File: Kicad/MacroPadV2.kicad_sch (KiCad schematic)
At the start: 31 parts, among them K1 KSW, K10 KSW, K11 KSW, K12 KSW, K2 KSW, K3 KSW, K4 KSW, K5 KSW, K6 KSW, K7 KSW, K8 KSW, K9 KSW, SW1 RotaryEncoder_Switch, U1 SparkFunProMicro

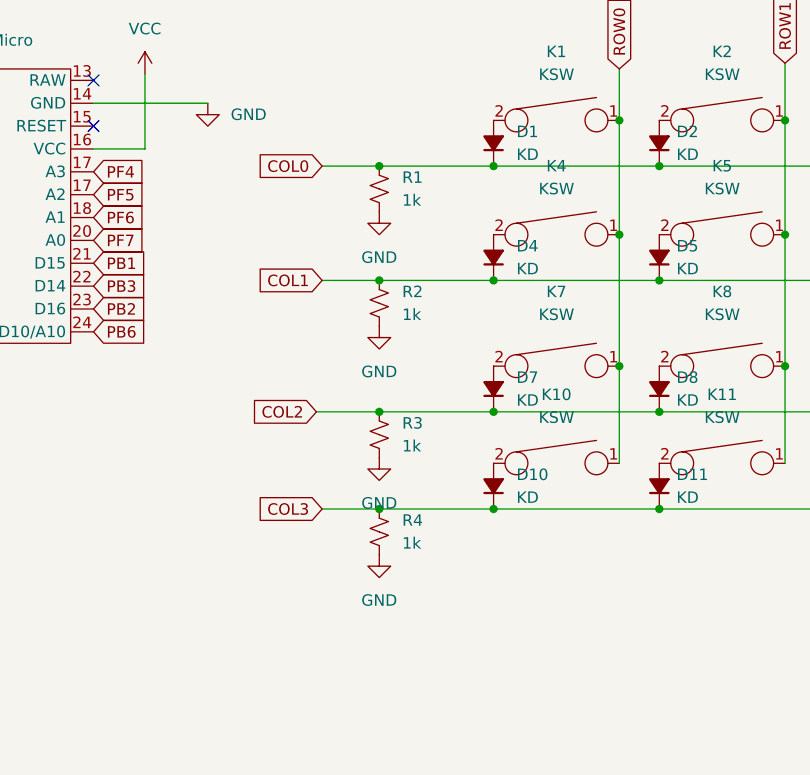
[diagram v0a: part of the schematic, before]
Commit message: Edit: IM AN IDIOT 	-ROWS ARE THE INPUTS, COLS ARE THE OUTPUTS 	-Set Cols Low to read a set, then all high after 	-Removed Pull down resistors on cols
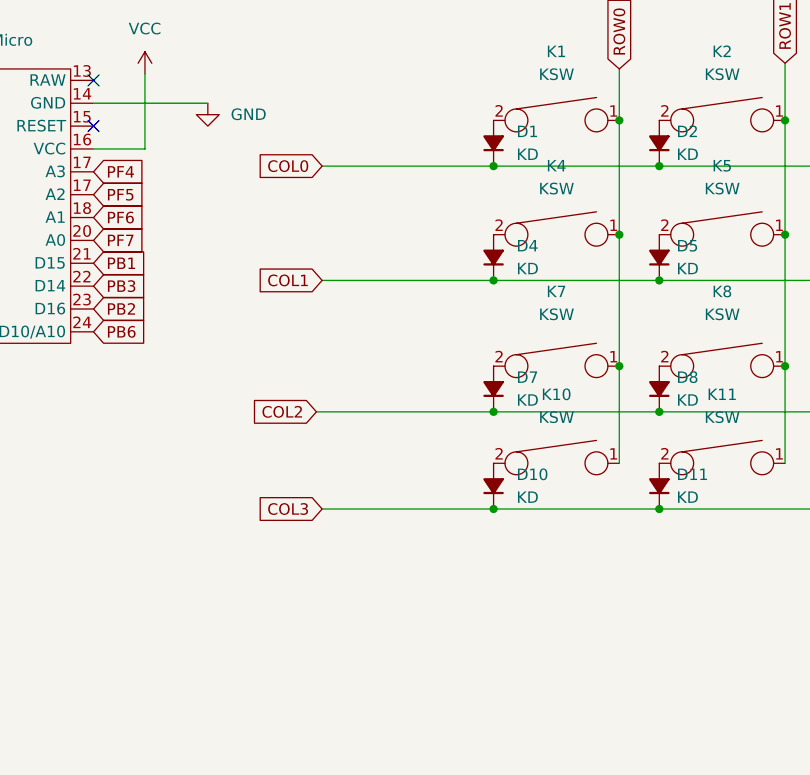
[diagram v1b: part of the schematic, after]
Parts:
- removed R1, R2, R3, R4: 1k, Resistor_SMD:R_0805_2012Metric_Pad1.20x1.40mm_HandSolder, symbol Device:R_Small_US
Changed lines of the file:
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@@
   (junction (at 120.65 29.21) (diameter 0) (color 0 0 0 0)
   )
-  (junction (at 93.98 72.39) (diameter 0) (color 0 0 0 0)
-  )
-  (junction (at 93.98 34.29) (diameter 0) (color 0 0 0 0)
-  )
   (junction (at 125.095 72.39) (diameter 0) (color 0 0 0 0)
   )
@@
   (junction (at 106.68 72.39) (diameter 0) (color 0 0 0 0)
   )
-  (junction (at 93.98 46.99) (diameter 0) (color 0 0 0 0)
-  )
   (junction (at 157.48 56.515) (diameter 0) (color 0 0 0 0)
-  )
-  (junction (at 93.98 61.595) (diameter 0) (color 0 0 0 0)
   )
   (junction (at 157.48 29.21) (diameter 0) (color 0 0 0 0)
@@
     (stroke (width 0) (type default) (color 0 0 0 0))
   )
-  (wire (pts (xy 93.98 72.39) (xy 106.68 72.39))
-    (stroke (width 0) (type default) (color 0 0 0 0))
-  )
   (wire (pts (xy 106.68 72.39) (xy 125.095 72.39))
     (stroke (width 0) (type default) (color 0 0 0 0))
@@
     (stroke (width 0) (type default) (color 0 0 0 0))
   )
-  (wire (pts (xy 93.98 46.99) (xy 106.68 46.99))
-    (stroke (width 0) (type default) (color 0 0 0 0))
-  )
   (wire (pts (xy 199.39 33.02) (xy 199.39 31.75))
     (stroke (width 0) (type default) (color 0 0 0 0))
   )
-  (wire (pts (xy 93.98 34.29) (xy 106.68 34.29))
-    (stroke (width 0) (type default) (color 0 0 0 0))
-  )
   (wire (pts (xy 157.48 41.91) (xy 157.48 56.515))
     (stroke (width 0) (type default) (color 0 0 0 0))
@@
     (stroke (width 0) (type default) (color 0 0 0 0))
   )
-  (wire (pts (xy 87.63 34.29) (xy 93.98 34.29))
+  (wire (pts (xy 87.63 34.29) (xy 106.68 34.29))
     (stroke (width 0) (type default) (color 0 0 0 0))
   )
@@
     (stroke (width 0) (type default) (color 0 0 0 0))
   )
-  (wire (pts (xy 87.63 46.99) (xy 93.98 46.99))
+  (wire (pts (xy 87.63 46.99) (xy 106.68 46.99))
     (stroke (width 0) (type default) (color 0 0 0 0))
   )
@@
     (stroke (width 0) (type default) (color 0 0 0 0))
   )
-  (wire (pts (xy 87.63 72.39) (xy 93.98 72.39))
+  (wire (pts (xy 87.63 72.39) (xy 106.68 72.39))
     (stroke (width 0) (type default) (color 0 0 0 0))
   )
@@
     (stroke (width 0) (type default) (color 0 0 0 0))
   )
-  (wire (pts (xy 86.995 61.595) (xy 93.98 61.595))
-    (stroke (width 0) (type default) (color 0 0 0 0))
-  )
-  (wire (pts (xy 93.98 61.595) (xy 106.68 61.595))
+  (wire (pts (xy 86.995 61.595) (xy 106.68 61.595))
     (stroke (width 0) (type default) (color 0 0 0 0))
   )
@@
     (pin "2")
   )
-  (symbol (lib_id "power:GND") (at 93.98 52.07 0) (unit 1)
-    (in_bom yes) (on_board yes) (fields_autoplaced)
-    (property "Reference" "#PWR0106" (id 0) (at 93.98 58.42 0)
-      (effects (font (size 1.27 1.27)) hide)
-    )
-    (property "Value" "GND" (id 1) (at 93.98 57.15 0))
-    (property "Footprint" "" (id 2) (at 93.98 52.07 0)
-      (effects (font (size 1.27 1.27)) hide)
-    )
-    (property "Datasheet" "" (id 3) (at 93.98 52.07 0)
-      (effects (font (size 1.27 1.27)) hide)
-    )
-    (pin "1")
-  )
   (symbol (lib_id "Device:D_Small_Filled") (at 125.095 31.75 90) (unit 1)
     (in_bom yes) (on_board yes) (fields_autoplaced)
@@
     (pin "1")
     (pin "2")
-  )
-  (symbol (lib_id "power:GND") (at 93.98 77.47 0) (unit 1)
-    (in_bom yes) (on_board yes) (fields_autoplaced)
-    (property "Reference" "#PWR0108" (id 0) (at 93.98 83.82 0)
-      (effects (font (size 1.27 1.27)) hide)
-    )
-    (property "Value" "GND" (id 1) (at 93.98 82.55 0))
-    (property "Footprint" "" (id 2) (at 93.98 77.47 0)
-      (effects (font (size 1.27 1.27)) hide)
-    )
-    (property "Datasheet" "" (id 3) (at 93.98 77.47 0)
-      (effects (font (size 1.27 1.27)) hide)
-    )
-    (pin "1")
   )
   (symbol (lib_id "macropad_parts:KSW") (at 119.38 36.83 0) (unit 1)
@@
     (pin "1")
   )
-  (symbol (lib_id "Device:R_Small_US") (at 93.98 36.83 0) (unit 1)
-    (in_bom yes) (on_board yes) (fields_autoplaced)
-    (property "Reference" "R1" (id 0) (at 96.52 35.5599 0)
-      (effects (font (size 1.27 1.27)) (justify left))
-    )
-    (property "Value" "1k" (id 1) (at 96.52 38.0999 0)
-      (effects (font (size 1.27 1.27)) (justify left))
-    )
-    (property "Footprint" "Resistor_SMD:R_0805_2012Metric_Pad1.20x1.40mm_HandSolder" (id 2) (at 93.98 36.83 0)
-      (effects (font (size 1.27 1.27)) hide)
-    )
-    (property "Datasheet" "~" (id 3) (at 93.98 36.83 0)
-      (effects (font (size 1.27 1.27)) hide)
-    )
-    (pin "1")
-    (pin "2")
-  )
   (symbol (lib_id "macropad_parts:KSW") (at 156.21 62.23 0) (unit 1)
     (in_bom yes) (on_board yes) (fields_autoplaced)
@@
     (pin "2")
   )
-  (symbol (lib_id "power:GND") (at 93.98 39.37 0) (unit 1)
-    (in_bom yes) (on_board yes) (fields_autoplaced)
-    (property "Reference" "#PWR0109" (id 0) (at 93.98 45.72 0)
-      (effects (font (size 1.27 1.27)) hide)
-    )
-    (property "Value" "GND" (id 1) (at 93.98 44.45 0))
-    (property "Footprint" "" (id 2) (at 93.98 39.37 0)
-      (effects (font (size 1.27 1.27)) hide)
-    )
-    (property "Datasheet" "" (id 3) (at 93.98 39.37 0)
-      (effects (font (size 1.27 1.27)) hide)
-    )
-    (pin "1")
-  )
   (symbol (lib_id "Device:R_Small_US") (at 200.025 40.64 0) (unit 1)
     (in_bom yes) (on_board yes) (fields_autoplaced)
@@
     )
     (property "Datasheet" "" (id 3) (at 137.795 51.435 0)
-      (effects (font (size 1.27 1.27)) hide)
-    )
-    (pin "1")
-    (pin "2")
-  )
-  (symbol (lib_id "Device:R_Small_US") (at 93.98 74.93 0) (unit 1)
-    (in_bom yes) (on_board yes) (fields_autoplaced)
-    (property "Reference" "R4" (id 0) (at 96.52 73.6599 0)
-      (effects (font (size 1.27 1.27)) (justify left))
-    )
-    (property "Value" "1k" (id 1) (at 96.52 76.1999 0)
-      (effects (font (size 1.27 1.27)) (justify left))
-    )
-    (property "Footprint" "Resistor_SMD:R_0805_2012Metric_Pad1.20x1.40mm_HandSolder" (id 2) (at 93.98 74.93 0)
-      (effects (font (size 1.27 1.27)) hide)
-    )
-    (property "Datasheet" "~" (id 3) (at 93.98 74.93 0)
       (effects (font (size 1.27 1.27)) hide)
     )
@@
     (pin "1")
   )
-  (symbol (lib_id "power:GND") (at 93.98 66.675 0) (unit 1)
-    (in_bom yes) (on_board yes) (fields_autoplaced)
-    (property "Reference" "#PWR0107" (id 0) (at 93.98 73.025 0)
-      (effects (font (size 1.27 1.27)) hide)
-    )
-    (property "Value" "GND" (id 1) (at 93.98 71.755 0))
-    (property "Footprint" "" (id 2) (at 93.98 66.675 0)
-      (effects (font (size 1.27 1.27)) hide)
-    )
-    (property "Datasheet" "" (id 3) (at 93.98 66.675 0)
-      (effects (font (size 1.27 1.27)) hide)
-    )
-    (pin "1")
-  )
   (symbol (lib_id "macropad_parts:KSW") (at 156.21 36.83 0) (unit 1)
     (in_bom yes) (on_board yes) (fields_autoplaced)
@@
     (pin "2")
   )
-  (symbol (lib_id "Device:R_Small_US") (at 93.98 49.53 0) (unit 1)
-    (in_bom yes) (on_board yes) (fields_autoplaced)
-    (property "Reference" "R2" (id 0) (at 96.52 48.2599 0)
-      (effects (font (size 1.27 1.27)) (justify left))
-    )
-    (property "Value" "1k" (id 1) (at 96.52 50.7999 0)
-      (effects (font (size 1.27 1.27)) (justify left))
-    )
-    (property "Footprint" "Resistor_SMD:R_0805_2012Metric_Pad1.20x1.40mm_HandSolder" (id 2) (at 93.98 49.53 0)
-      (effects (font (size 1.27 1.27)) hide)
-    )
-    (property "Datasheet" "~" (id 3) (at 93.98 49.53 0)
-      (effects (font (size 1.27 1.27)) hide)
-    )
-    (pin "1")
-    (pin "2")
-  )
   (symbol (lib_id "Device:D_Small_Filled") (at 143.51 69.85 90) (unit 1)
     (in_bom yes) (on_board yes) (fields_autoplaced)
@@
     )
     (property "Datasheet" "~" (id 3) (at 106.68 44.45 90)
-      (effects (font (size 1.27 1.27)) hide)
-    )
-    (pin "1")
-    (pin "2")
-  )
-  (symbol (lib_id "Device:R_Small_US") (at 93.98 64.135 0) (unit 1)
-    (in_bom yes) (on_board yes) (fields_autoplaced)
-    (property "Reference" "R3" (id 0) (at 96.52 62.8649 0)
-      (effects (font (size 1.27 1.27)) (justify left))
-    )
-    (property "Value" "1k" (id 1) (at 96.52 65.4049 0)
-      (effects (font (size 1.27 1.27)) (justify left))
-    )
-    (property "Footprint" "Resistor_SMD:R_0805_2012Metric_Pad1.20x1.40mm_HandSolder" (id 2) (at 93.98 64.135 0)
-      (effects (font (size 1.27 1.27)) hide)
-    )
-    (property "Datasheet" "~" (id 3) (at 93.98 64.135 0)
       (effects (font (size 1.27 1.27)) hide)
     )
@@
       (reference "#PWR0105") (unit 1) (value "VCC") (footprint "")
     )
-    (path "/16c6adea-2c09-487f-b444-72a19e0d51f6"
-      (reference "#PWR0106") (unit 1) (value "GND") (footprint "")
-    )
-    (path "/beeb0ef5-90f2-4657-bbfb-e4ec5108bd51"
-      (reference "#PWR0107") (unit 1) (value "GND") (footprint "")
-    )
-    (path "/27e91b9a-6f37-4b94-aa0e-6c8f69ad38c6"
-      (reference "#PWR0108") (unit 1) (value "GND") (footprint "")
-    )
-    (path "/8c76f0ee-46bf-48da-a1a4-40848f3341e7"
-      (reference "#PWR0109") (unit 1) (value "GND") (footprint "")
-    )
     (path "/477a2da7-653c-46b0-ba45-02374d68f85b"
       (reference "#PWR0110") (unit 1) (value "GND") (footprint "")
@@
       (reference "K12") (unit 1) (value "KSW") (footprint "aarohanl:CherryMxFP")
     )
-    (path "/6478625c-21e4-4662-9bca-73f0eb42d564"
-      (reference "R1") (unit 1) (value "1k") (footprint "Resistor_SMD:R_0805_2012Metric_Pad1.20x1.40mm_HandSolder")
-    )
-    (path "/d6c8f921-dae6-47f5-9584-b961d8f837c1"
-      (reference "R2") (unit 1) (value "1k") (footprint "Resistor_SMD:R_0805_2012Metric_Pad1.20x1.40mm_HandSolder")
-    )
-    (path "/f1b66b01-c0bc-4afd-af81-8e0a5087191b"
-      (reference "R3") (unit 1) (value "1k") (footprint "Resistor_SMD:R_0805_2012Metric_Pad1.20x1.40mm_HandSolder")
-    )
-    (path "/9657d074-22c5-4a09-9ef8-ad7ad64cd41d"
-      (reference "R4") (unit 1) (value "1k") (footprint "Resistor_SMD:R_0805_2012Metric_Pad1.20x1.40mm_HandSolder")
-    )
     (path "/8e24a180-e267-4f0c-9524-fbe559bd83b8"

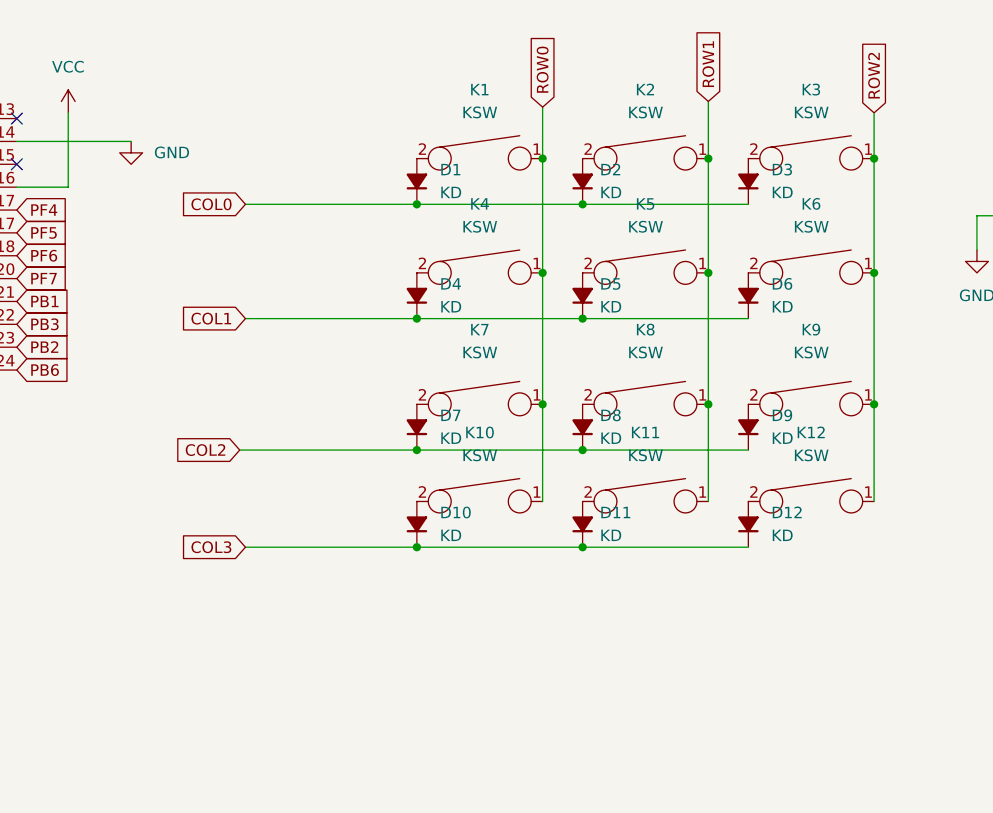
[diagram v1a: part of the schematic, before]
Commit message: V2 Schem and Routing Complete for drop in micro pro, making new branch for STM32F103
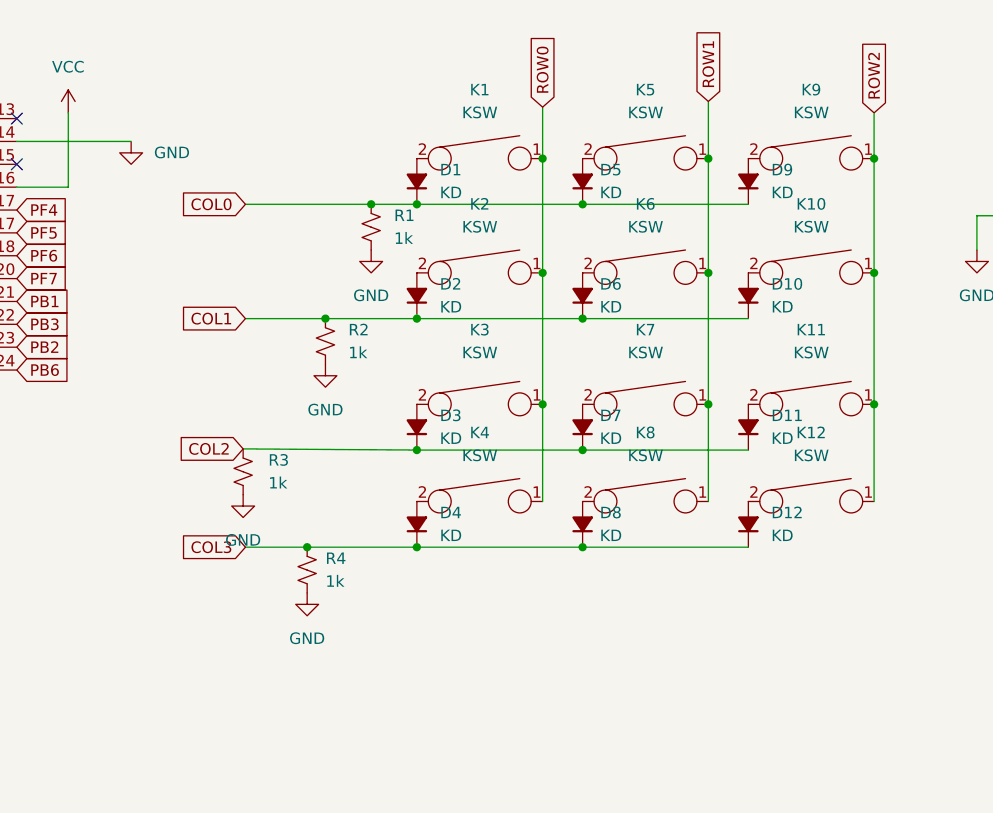
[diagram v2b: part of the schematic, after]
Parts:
- added R1, R2, R3, R4: 1k, Resistor_SMD:R_0805_2012Metric_Pad1.20x1.40mm_HandSolder, symbol Device:R_Small_US
- renumbered D6 to D10, D9 to D11, D4 to D2, D7 to D3, D10 to D4, D2 to D5, D5 to D6, D8 to D7, D11 to D8, D3 to D9, K6 to K10, K9 to K11, K4 to K2, K7 to K3, K10 to K4, K2 to K5, K5 to K6, K8 to K7, K11 to K8, K3 to K9
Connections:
- net COL0: now also R1.1
- net COL1: now also R2.1
- net COL2: now also R3.1
- net COL3: now also R4.1
- net GND: now also R1.2, R2.2, R3.2, R4.2

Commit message: New LAyout an Routing done
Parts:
- removed D1, D10, D11, D12, D2, D3, D4, D5, D6, D7, D8, D9: KD, mpadfps:sod323, symbol Device:D_Small_Filled
- removed U1: SparkFunProMicro, aarohanl:SparkFrunProMicro, symbol macropad_parts:SparkFunProMicro
- added C1, C2: 15pF, Capacitor_SMD:C_0805_2012Metric_Pad1.18x1.45mm_HandSolder, symbol Device:C_Small
- added C3, C4, C5: 100nF, Capacitor_SMD:C_0805_2012Metric_Pad1.18x1.45mm_HandSolder, symbol Device:C_Small
- added C6: 1uF, Capacitor_SMD:C_0805_2012Metric_Pad1.18x1.45mm_HandSolder, symbol Device:C_Small
- added C7, C8, C9: 4.7uF, Capacitor_SMD:C_0805_2012Metric_Pad1.18x1.45mm_HandSolder, symbol Device:C_Small
- added D1: D, Diode_SMD:D_0805_2012Metric_Pad1.15x1.40mm_HandSolder, symbol Device:D
- added D10, D11, D12, D13, D2, D3, D4, D5, D6, D7, D8, D9: 1N4148WX-TP, Diode_SMD:D_0805_2012Metric_Pad1.15x1.40mm_HandSolder, symbol symbols:1N4148WX-TP
- added F1: OZCH, mpadfps:OZCHFusr, symbol Device:Polyfuse_Small
- added J1, J2, J4: 3PinJump, Connector_PinHeader_2.54mm:PinHeader_1x03_P2.54mm_Vertical, symbol macropad_parts:3PinJump
- added J3: GCT-USB4085, mpadfps:USB4085-GF-A, symbol symbols:GCT-USB4085
- added J5, J6: 4PinJump, Connector_PinHeader_2.54mm:PinHeader_1x04_P2.54mm_Vertical, symbol macropad_parts:4PinJump
- added R6, R7, R8, R9: 1k, Resistor_SMD:R_0805_2012Metric_Pad1.20x1.40mm_HandSolder, symbol Device:R_Small_US
- added SW1, SW2: SWITCH_TACTILE_SPST-NO_0.05A_12V, mpadfps:PTS645-G, symbol macropad_parts:SWITCH_TACTILE_SPST-NO_0.05A_12V
- added U1: STM32F103C8T6TR, mpadfps:LQFP48, symbol symbols:STM32F103C8T6TR
- added U2: AP2114HA-3.3TRG1, keyboard_fp:SOT-223_DIO-L, symbol macropad_parts:AP2114HA-3.3TRG1
- added X1: TSX-3225_16.0000MF18X-AC6, mpadfps:TSX-3226, symbol macropad_parts:TSX-3225_16.0000MF18X-AC6
- K1, K10, K11, K12, K2, K3, K4, K5, K6, K7, K8, K9: footprint aarohanl:CherryMxFP -> keyboard_fp:CherryMx
- R1, R2, R4: value 1k -> 10k
- R3, R5: value 1k -> 5.1k
- SW3: renamed from SW1; footprint aarohanl:PEC11H4020FS0016_PinCorrection -> mpadfps:PEC11H-RotaryEncoderSwitch
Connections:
- net COL0: now also K1.1, K10.1, K4.1, K7.1, U1.14 (PA4); no longer R1.1
- net COL1: now also K11.1, K2.1, K5.1, K8.1, U1.15 (PA5); no longer R2.1
- net COL2: now also K12.1, K3.1, K6.1, K9.1, U1.16 (PA6); no longer R3.1
- net GND: now also R3.1, R5.1, C1.1, C2.2, C3.2, C4.2, C5.2, C6.2, C7.2, C8.1, C9.2, J3.A1 (GND), J3.A12 (GND), J3.B1 (GND), J3.B12 (GND), J3.SHELL (GND), J4.2, J6.4, R6.1, R7.1, R8.1, R9.1, SW1.3, SW1.4, SW2.3, SW2.4, U1.23 (VSS_1), U1.35 (VSS_2), U1.47 (VSS_3), U1.8 (VSSA), U2.2 (GND), U2.4 (GND), X1.2 (GND), X1.4 (GND); no longer R2.2, R3.2, R5.2
- net ROW0: now also D13.2, D5.2, D6.2, R9.2, U1.10 (PA0); no longer K1.1, K2.1, K3.1, K4.1
- net ROW1: now also D10.2, D2.2, D7.2, R8.2, U1.11 (PA1); no longer K5.1, K6.1, K7.1, K8.1
- net ROW2: now also D11.2, D3.2, D8.2, R7.2, U1.12 (PA2); no longer K10.1, K11.1, K12.1, K9.1
- net at K8.2: now also D8.1
- net at K5.2: now also D7.1
- net at K2.2: now also D6.1
- net at K10.2: now also D4.1
- net at K12.2: now also D12.1
- net at K6.2: now also D10.1
- net at K4.2: now also D2.1
- net at K1.2: now also D5.1
- net at K7.2: now also D3.1
- net at K9.2: now also D11.1
- net at K11.2: now also D9.1
- net at K3.2: now also D13.1
- net COL3: no longer names the net of R4.1
- net COL3: now also J2.3
- net PD4 renamed ENCSW
- net ENCSW: now also U1.2 (PC13); no longer R5.1
- net PF6 renamed ENCB
- net ENCB: now also U1.4 (PC15)
- net PF7 renamed ENCA
- net ENCA: now also U1.3 (PC14)
- net VCC renamed +3V3
- net +3V3: now also R2.1, C4.1, C5.1, C6.1, C7.1, C8.2, J1.1, J2.1, J4.1, J6.1, U1.1 (VBAT), U1.24 (VDD_1), U1.36 (VDD_2), U1.48 (VDD_3), U1.9 (VDDA), U2.3 (VOUT)
- new net: C1.2, U1.5 (OSC_IN), X1.1 (In)
- new net: J3.B5 (CC2), R5.2
- new net: J3.A5 (CC1), R3.2
- new net: C2.1, U1.6 (OSC_OUT), X1.3 (OUT)
- new net: D1.1 (K), F1.1
- new net: J1.3, R1.1
- new net +5V: C9.1, F1.2, J4.3, U2.1 (VIN)
- new net BOOT0: J2.2, J5.1, U1.44 (BOOT0)
- new net BOOT1: J1.2, J5.2, U1.20 (PB2)
- new net D+: J3.A6 (D+1), J3.B6 (D+2), U1.33 (PA12)
- new net D-: J3.A7 (D-1), J3.B7 (D-2), U1.32 (PA11)
- new net MODE: SW1.1, SW1.2, U1.18 (PB0)
- new net NRST: C3.1, J5.4, R2.2, SW2.1, SW2.2, U1.7 (NRST)
- new net ROW3: D12.2, D4.2, D9.2, R6.2, U1.13 (PA3)
- new net SCL: U1.42 (PB6)
- new net SDA: U1.41 (PB5)
- new net SWCLK: J6.3, U1.38 (PA15)
- new net SWDIO: J6.2, U1.37 (PA14)
- new net TraceSWO: J5.3, U1.39 (PB3)
- new net VBUS: D1.2 (A), J3.A4 (VBUS), J3.A9 (VBUS), J3.B4 (VBUS), J3.B9 (VBUS)
- no-connect marks 10 -> 2
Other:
- moved on the sheet: K1, SW3
